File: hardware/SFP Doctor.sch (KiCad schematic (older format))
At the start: 16 parts, among them J1 1888247-1, P1 CONN_01X26, P2 CONN_01X26, U1 TSR_1-2433, U2 PCA9306

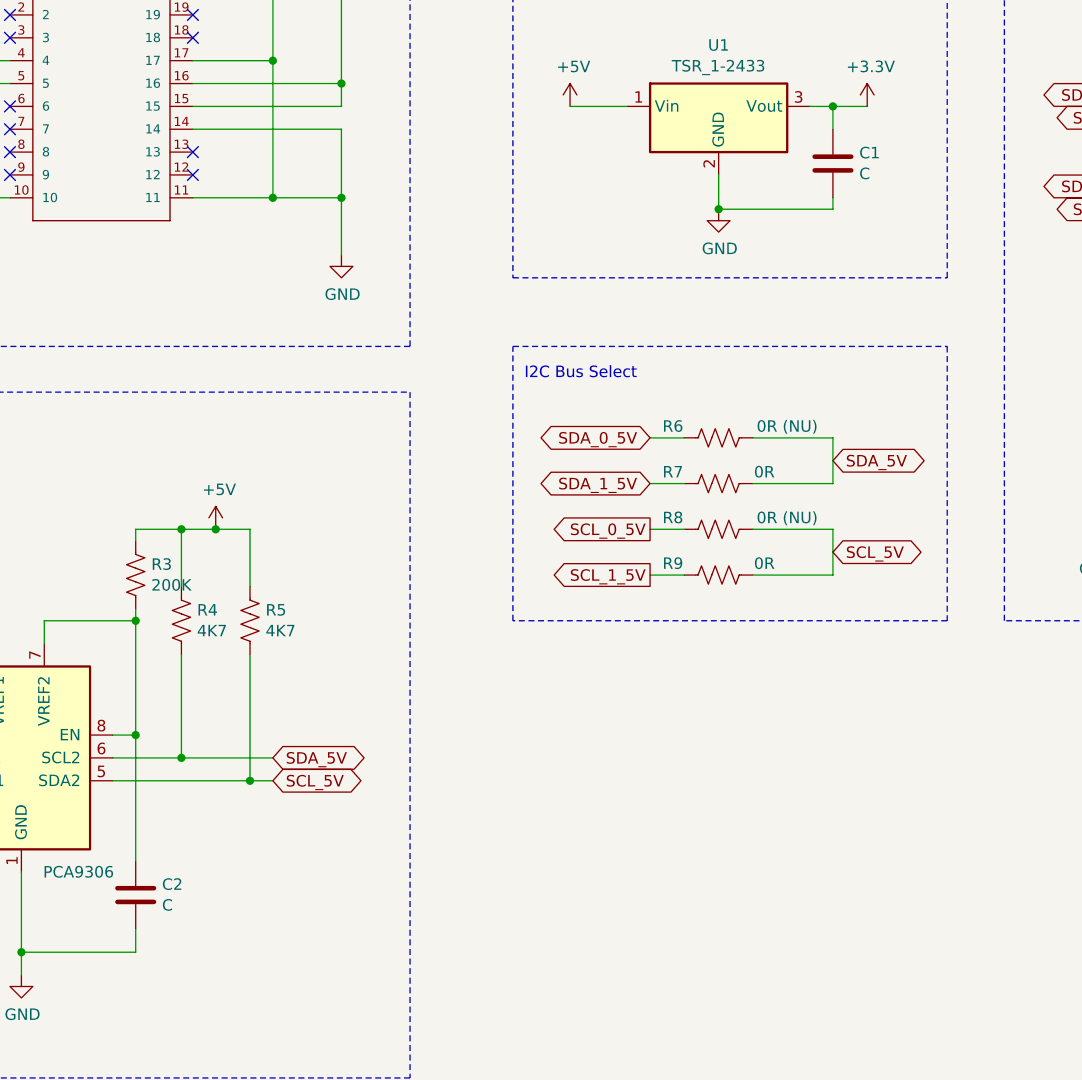
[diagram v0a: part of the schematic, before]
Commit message: chore: updated schematic
Missing capacitor values added
Logos added to schematic
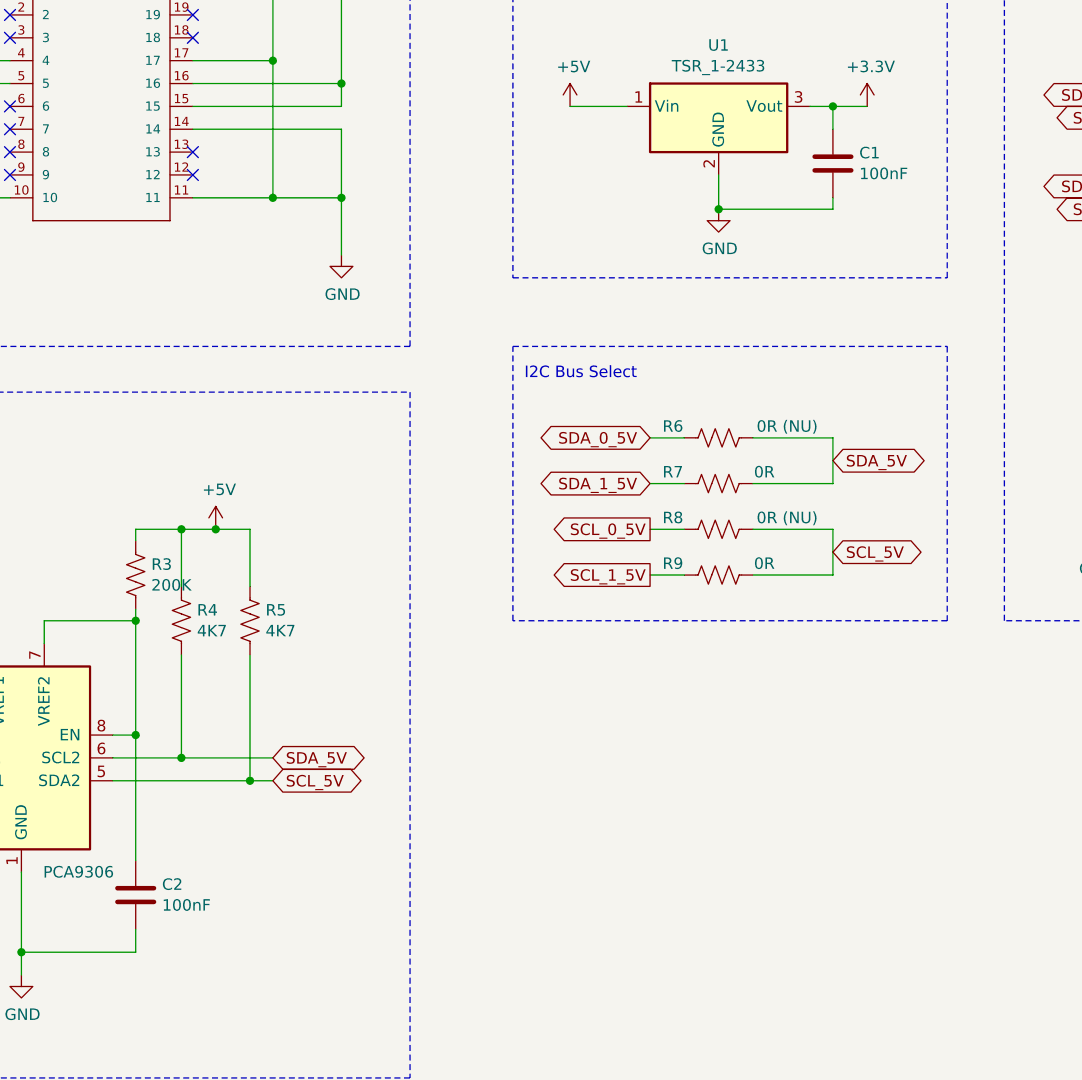
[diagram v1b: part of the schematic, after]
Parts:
- C1, C2: value C -> 100nF

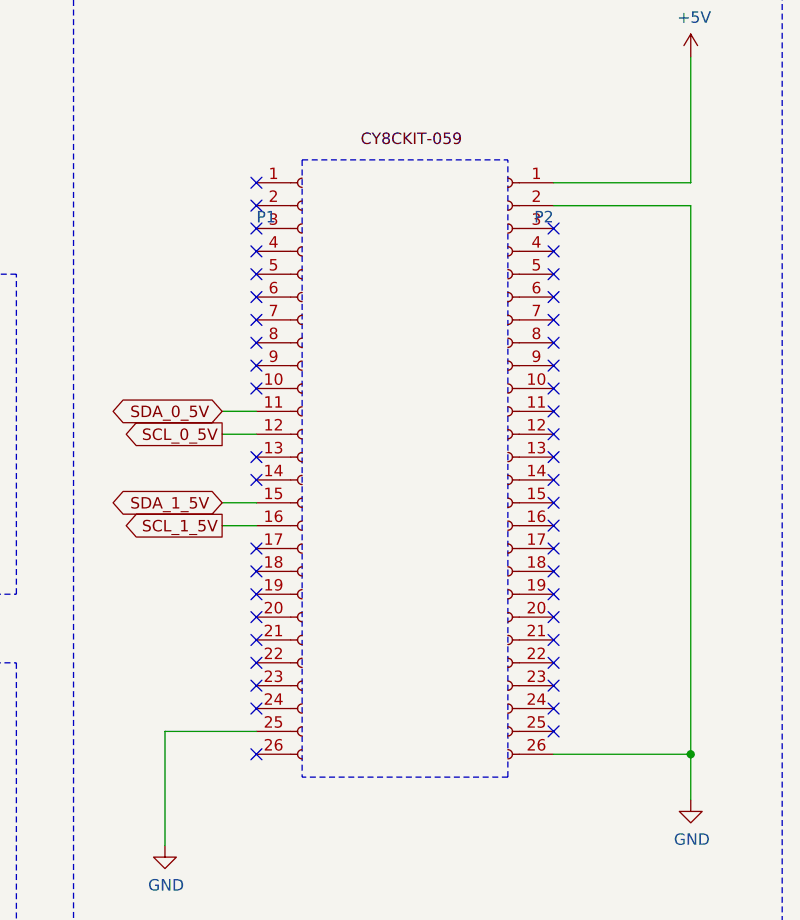
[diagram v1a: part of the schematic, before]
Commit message: chore(hardware): added pin labels
added pin labels to the CYC8CKIT-059 symbol
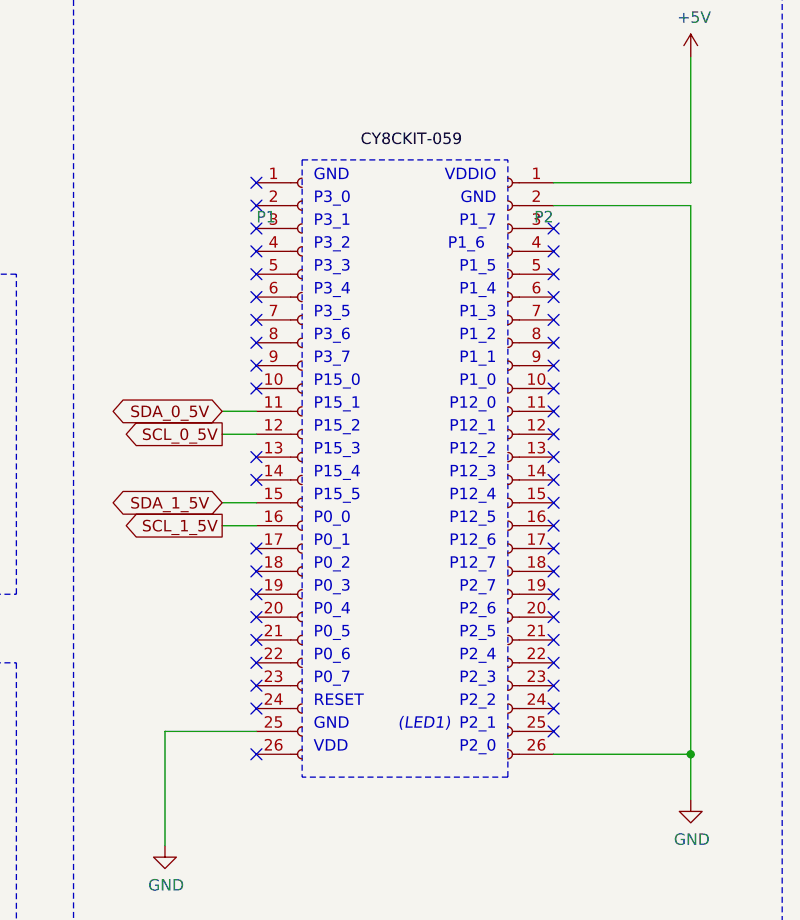
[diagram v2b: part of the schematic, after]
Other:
- note added: "(LED1)"
- note added: "GND"
- note added: "P0_0"
- note added: "P0_1"
- note added: "P0_2"
- note added: "P0_3"
- note added: "P0_4"
- note added: "P0_5"
- note added: "P0_6"
- note added: "P0_7"
- note added: "P12_0"
- note added: "P12_1"
- note added: "P12_2"
- note added: "P12_3"
- note added: "P12_4"
- note added: "P12_5"
- note added: "P12_6"
- note added: "P12_7"
- note added: "P15_0"
- note added: "P15_1"
- note added: "P15_2"
- note added: "P15_3"
- note added: "P15_4"
- note added: "P15_5"
- note added: "P1_0"
- note added: "P1_1"
- note added: "P1_2"
- note added: "P1_3"
- note added: "P1_4"
- note added: "P1_5"
- note added: "P1_6"
- note added: "P1_7"
- note added: "P2_0"
- note added: "P2_1"
- note added: "P2_2"
- note added: "P2_3"
- note added: "P2_4"
- note added: "P2_5"
- note added: "P2_6"
- note added: "P2_7"
- note added: "P3_0"
- note added: "P3_1"
- note added: "P3_2"
- note added: "P3_3"
- note added: "P3_4"
- note added: "P3_5"
- note added: "P3_6"
- note added: "P3_7"
- note added: "RESET"
- note added: "VDD"
- note added: "VDDIO"
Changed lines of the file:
@@
 EndData
 $EndBitmap
+Text Notes 8550 4500 0    50   ~ 0
+VDD
+Text Notes 8550 4400 0    50   ~ 0
+GND
+Text Notes 8550 4200 0    50   ~ 0
+P0_7
+Text Notes 8550 4100 0    50   ~ 0
+P0_6
+Text Notes 8550 4000 0    50   ~ 0
+P0_5
+Text Notes 8550 3900 0    50   ~ 0
+P0_4
+Text Notes 8550 3800 0    50   ~ 0
+P0_3
+Text Notes 8550 3700 0    50   ~ 0
+P0_2
+Text Notes 8550 3600 0    50   ~ 0
+P0_1
+Text Notes 8550 3500 0    50   ~ 0
+P0_0
+Text Notes 8550 3400 0    50   ~ 0
+P15_5
+Text Notes 8550 3300 0    50   ~ 0
+P15_4
+Text Notes 8550 3200 0    50   ~ 0
+P15_3
+Text Notes 8550 3100 0    50   ~ 0
+P15_2
+Text Notes 8550 3000 0    50   ~ 0
+P15_1
+Text Notes 8550 2900 0    50   ~ 0
+P15_0
+Text Notes 8550 2800 0    50   ~ 0
+P3_7
+Text Notes 8550 2700 0    50   ~ 0
+P3_6
+Text Notes 8550 2600 0    50   ~ 0
+P3_5
+Text Notes 8550 2500 0    50   ~ 0
+P3_4
+Text Notes 8550 2400 0    50   ~ 0
+P3_3
+Text Notes 8550 2300 0    50   ~ 0
+P3_2
+Text Notes 8550 2200 0    50   ~ 0
+P3_1
+Text Notes 8550 2100 0    50   ~ 0
+P3_0
+Text Notes 8550 2000 0    50   ~ 0
+GND
+Text Notes 8550 4300 0    50   ~ 0
+RESET
+Text Notes 9350 2000 2    50   ~ 0
+VDDIO
+Text Notes 9350 2100 2    50   ~ 0
+GND
+Text Notes 9350 2200 2    50   ~ 0
+P1_7
+Text Notes 9300 2300 2    50   ~ 0
+P1_6
+Text Notes 9350 2400 2    50   ~ 0
+P1_5
+Text Notes 9350 2500 2    50   ~ 0
+P1_4
+Text Notes 9350 2600 2    50   ~ 0
+P1_3
+Text Notes 9350 2700 2    50   ~ 0
+P1_2
+Text Notes 9350 2800 2    50   ~ 0
+P1_1
+Text Notes 9350 2900 2    50   ~ 0
+P1_0
+Text Notes 9350 3000 2    50   ~ 0
+P12_0
+Text Notes 9350 3100 2    50   ~ 0
+P12_1
+Text Notes 9350 3200 2    50   ~ 0
+P12_2
+Text Notes 9350 3300 2    50   ~ 0
+P12_3
+Text Notes 9350 3400 2    50   ~ 0
+P12_4
+Text Notes 9350 3500 2    50   ~ 0
+P12_5
+Text Notes 9350 3600 2    50   ~ 0
+P12_6
+Text Notes 9350 3700 2    50   ~ 0
+P12_7
+Text Notes 9350 3800 2    50   ~ 0
+P2_7
+Text Notes 9350 3900 2    50   ~ 0
+P2_6
+Text Notes 9350 4000 2    50   ~ 0
+P2_5
+Text Notes 9350 4100 2    50   ~ 0
+P2_4
+Text Notes 9350 4200 2    50   ~ 0
+P2_3
+Text Notes 9350 4300 2    50   ~ 0
+P2_2
+Text Notes 9350 4400 2    50   ~ 0
+P2_1
+Text Notes 9350 4500 2    50   ~ 0
+P2_0
+Text Notes 9150 4400 2    50   Italic 0
+(LED1)
 $EndSCHEMATC

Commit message: wip: revision 1.2 of PCB
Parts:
- removed J1: 1888247-1, 1888247-1:TE_1888247-1, symbol 1888247-1:1888247-1
- removed R6, R8: 0R (NU), Resistor_SMD:R_1206_3216Metric_Pad1.42x1.75mm_HandSolder, symbol Device:R_US
- removed R7, R9: 0R, Resistor_SMD:R_1206_3216Metric_Pad1.42x1.75mm_HandSolder, symbol Device:R_US
- added D1, D2, D3: APA102, LED_SMD:LED_RGB_5050-6, symbol LED:APA102
- added J1: 2227023-1, 2227023-1:TE_2227023-1, symbol 2227023-1:2227023-1
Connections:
- net SCL_1_5V is gone; now on net SCL_5V: P1.16 (Pin_16)
- net SDA_1_5V is gone; now on net SDA_5V: P1.15 (Pin_15)
- net +3V3: now also J1.15, J1.16
- net +5V: now also D1.4 (VCC), D2.4 (VCC), D3.4 (VCC)
- net GND: now also D1.3 (GND), D2.3 (GND), D3.3 (GND), J1.1, J1.10, J1.11, J1.14, J1.17, J1.20, J1.S1 (SHIELD), J1.S10 (SHIELD), J1.S11 (SHIELD), J1.S12 (SHIELD), J1.S13 (SHIELD), J1.S14 (SHIELD), J1.S15 (SHIELD), J1.S16 (SHIELD), J1.S17 (SHIELD), J1.S18 (SHIELD), J1.S19 (SHIELD), J1.S2 (SHIELD), J1.S20 (SHIELD), J1.S3 (SHIELD), J1.S4 (SHIELD), J1.S5 (SHIELD), J1.S6 (SHIELD), J1.S7 (SHIELD), J1.S8 (SHIELD), J1.S9 (SHIELD)
- net SCL_3V3: now also J1.5
- net SDA_3V3: now also J1.4
- net LED_CLOCK: now reaches P1.22 (Pin_22)
- net LED_CLOCK: now also D1.2 (CI)
- net LED_DATA: now reaches P1.23 (Pin_23)
- net LED_DATA: now also D1.1 (DI)
- net SCL_0_5V: no longer names the net of P1.12 (Pin_12)
- net SDA_0_5V: no longer names the net of P1.11 (Pin_11)
- new net: D1.5 (CO), D2.2 (CI)
- new net: D1.6 (DO), D2.1 (DI)
- new net: D2.5 (CO), D3.2 (CI)
- new net: D2.6 (DO), D3.1 (DI)
- no-connect marks 54 -> 56
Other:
- note added: "LEDS"
- note removed: "I2C Bus Select"
- note removed: "SFP Connector"
- moved on the sheet: C1, C2, P1, P2, R1, R2, R3, R4, R5, U1, U2

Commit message: wip: revision 1.3 of PCB
Moved SFP cage
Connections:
- net LED_CLOCK: now also P2.12 (Pin_12); no longer P1.22 (Pin_22)
- net LED_DATA: now also P2.11 (Pin_11); no longer P1.23 (Pin_23)
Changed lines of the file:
@@
 EESchema Schematic File Version 4
+LIBS:SFP Doctor-cache
 EELAYER 30 0
 EELAYER END
@@
 Title "SFP Doctor"
 Date "2019-11-11"
-Rev "1.2"
+Rev "1.3"
 Comp "fizzyade.com"
 Comment1 ""
@@
 Wire Wire Line
 	9250 2050 9850 2050
-Text GLabel 7800 3450 0    50   BiDi ~ 0
-SDA_5V
-Wire Wire Line
-	7800 3450 7950 3450
-Wire Wire Line
-	7800 3550 7950 3550
 $Comp
 L power:GND #PWR0108
@@
 Text GLabel 2750 3000 0    50   Input ~ 0
 SCL_3V3
-Text GLabel 7800 3550 0    50   Output ~ 0
-SCL_5V
 Wire Wire Line
 	2850 3500 2300 3500
@@
 NoConn ~ 9250 3450
 NoConn ~ 9250 3350
-NoConn ~ 9250 3250
-NoConn ~ 9250 3150
-NoConn ~ 9250 3050
 NoConn ~ 9250 2950
 NoConn ~ 9250 2850
@@
 NoConn ~ 5950 6650
 NoConn ~ 6050 6650
-Text GLabel 7800 4150 0    50   Output ~ 0
+Text GLabel 9350 3150 2    50   Output ~ 0
 LED_CLOCK
-Text GLabel 7800 4250 0    50   Output ~ 0
+Text GLabel 9350 3050 2    50   Output ~ 0
 LED_DATA
-Wire Wire Line
-	7800 4150 7950 4150
-Wire Wire Line
-	7950 4250 7800 4250
 NoConn ~ 7950 3750
 NoConn ~ 7950 3650
 NoConn ~ 7950 4350
+Text GLabel 7800 3550 0    50   Output ~ 0
+SCL_5V
+Wire Wire Line
+	7800 3550 7950 3550
+Wire Wire Line
+	7800 3450 7950 3450
+Text GLabel 7800 3450 0    50   BiDi ~ 0
+SDA_5V
+Wire Wire Line
+	9250 3050 9350 3050
+Wire Wire Line
+	9250 3150 9350 3150
+NoConn ~ 7950 4150
+NoConn ~ 7950 4250
+NoConn ~ 9250 3250
 $EndSCHEMATC
